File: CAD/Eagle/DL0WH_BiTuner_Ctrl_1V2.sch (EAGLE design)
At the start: 157 parts, among them Q0321 ABS07-32.768KHZ, U0101 STM32L476RXT_64PIN_LDO, U0601 MC33996, U0701 MC33996, U0801 MC33996, U0921 TS5A23166, U0941 LM2611, U0951 OPA354, U0961 OPA354, U0962 MCP4661-103E-MS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

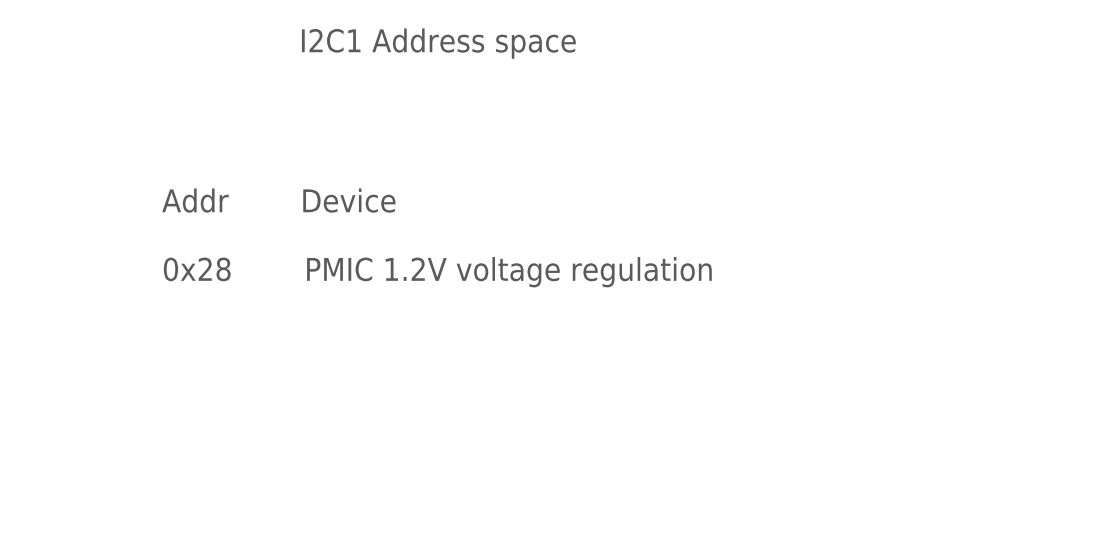
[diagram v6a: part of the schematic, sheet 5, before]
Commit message: HW_1V2 - CAD/Eagle - I2C address of dig.poti fixed to 0x14
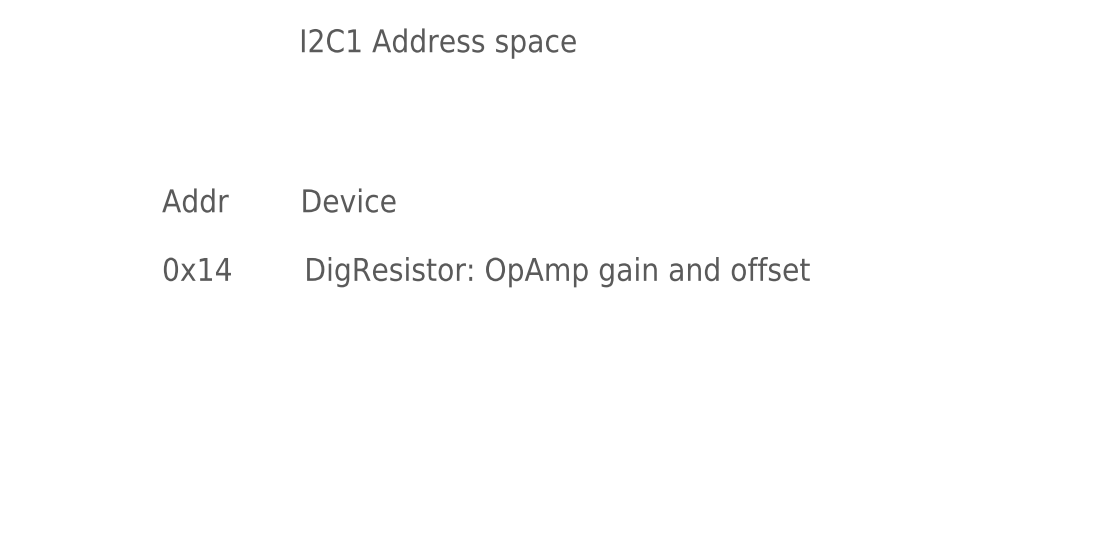
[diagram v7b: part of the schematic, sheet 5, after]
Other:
- note added: "Addr Device 0x14 DigResistor: OpAmp gain and offset"
- note removed: "Addr Device 0x28 PMIC 1.2V voltage regulation"
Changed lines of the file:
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@@
 <plain>
 <text x="134.62" y="137.16" size="2.54" layer="97" ratio="15">Addr        Device
-0x28        PMIC 1.2V voltage regulation
+0x14        DigResistor: OpAmp gain and offset
 </text>
 <text x="22.86" y="162.56" size="2.54" layer="97" ratio="15">I2C1 Termination</text>

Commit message: HW_1V2 - CAD/Eagle - wrong I2C address fixed
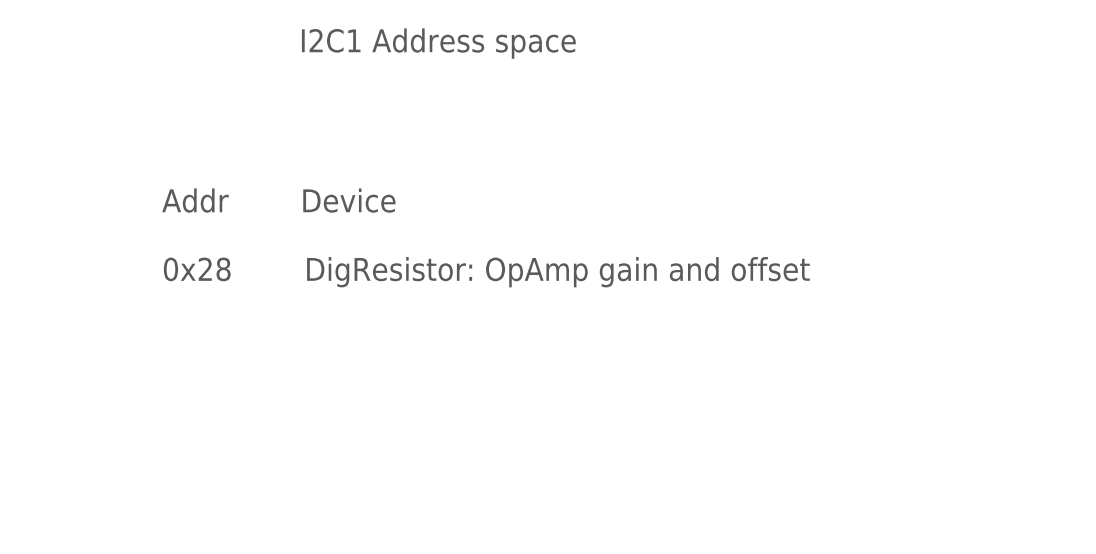
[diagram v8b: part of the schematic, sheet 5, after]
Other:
- note added: "Addr Device 0x28 DigResistor: OpAmp gain and offset"
- note removed: "Addr Device 0x14 DigResistor: OpAmp gain and offset"
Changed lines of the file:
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@@
 <plain>
 <text x="134.62" y="137.16" size="2.54" layer="97" ratio="15">Addr        Device
-0x14        DigResistor: OpAmp gain and offset
+0x28        DigResistor: OpAmp gain and offset
 </text>
 <text x="22.86" y="162.56" size="2.54" layer="97" ratio="15">I2C1 Termination</text>
